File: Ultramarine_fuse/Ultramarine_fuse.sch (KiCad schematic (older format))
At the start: 122 parts, among them J1 Conn_01x04_Female, J2 Conn_01x04_Female, SW1 SW_Push, SW10 SW_Push, SW11 SW_Push, SW12 SW_Push, SW13 SW_Push, SW14 SW_Push, SW15 SW_Push, SW16 SW_Push, SW17 SW_Push, SW18 SW_Push, SW19 SW_Push, SW2 SW_Push, SW20 SW_Push, SW21 SW_Push, SW22 SW_Push, SW23 SW_Push, SW24 SW_Push, SW25 SW_Push, SW26 SW_Push, SW27 SW_Push, SW28 SW_Push, SW29 SW_Push, SW3 SW_Push, SW30 SW_Push, SW31 SW_Push, SW32 SW_Push, SW33 SW_Push, SW34 SW_Push, SW35 SW_Push, SW36 SW_Push, SW4 SW_Push, SW5 SW_Push, SW6 SW_Push, SW7 SW_Push, SW8 SW_Push, SW9 SW_Push, U1 Pro_Micro, U10 SK6812mini, U11 SK6812mini, U12 SK6812mini, U13 SK6812mini, U14 SK6812mini, U15 SK6812mini, U16 SK6812mini, U17 SK6812mini, U18 SK6812mini, U19 SK6812mini, U2 SK6812mini, U20 SK6812mini, U21 SK6812mini, U22 SK6812mini, U23 SK6812mini, U24 SK6812mini, U25 SK6812mini, U26 SK6812mini, U27 SK6812mini, U28 SK6812mini, U29 SK6812mini, U3 SK6812mini, U30 SK6812mini, U31 SK6812mini, U32 SK6812mini, U33 SK6812mini, U34 SK6812mini, U35 SK6812mini, U36 SK6812mini, U4 SK6812mini, U5 SK6812mini, U6 SK6812mini, U7 SK6812mini, U8 SK6812mini, U9 SK6812mini

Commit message: nothing special
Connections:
- net Col0: now also SW1.1, SW15.1, SW22.1, SW8.1
- net Col1: now also SW16.1, SW2.1, SW23.1, SW9.1
- net Col2: now also SW10.1, SW17.1, SW24.1, SW3.1
- net Col3: now also SW11.1, SW18.1, SW25.1, SW4.1
- net Col4: now also SW12.1, SW19.1, SW26.1, SW5.1
- net Col5: now also SW13.1, SW20.1, SW27.1, SW6.1
- net Col6: now also SW14.1, SW21.1, SW28.1, SW7.1
- net GND: now also U10.2 (GND), U11.2 (GND), U12.2 (GND), U13.2 (GND), U14.2 (GND), U15.2 (GND), U23.2 (GND), U24.2 (GND), U25.2 (GND), U26.2 (GND), U27.2 (GND), U28.2 (GND), U29.2 (GND), U31.2 (GND), U32.2 (GND), U33.2 (GND), U34.2 (GND), U35.2 (GND), U36.2 (GND)
- net VCC: now also U10.4 (VCC), U11.4 (VCC), U12.4 (VCC), U13.4 (VCC), U14.4 (VCC), U15.4 (VCC), U23.4 (VCC), U24.4 (VCC), U25.4 (VCC), U26.4 (VCC), U27.4 (VCC), U28.4 (VCC), U29.4 (VCC), U3.4 (VCC), U4.4 (VCC), U5.4 (VCC), U6.4 (VCC), U7.4 (VCC)

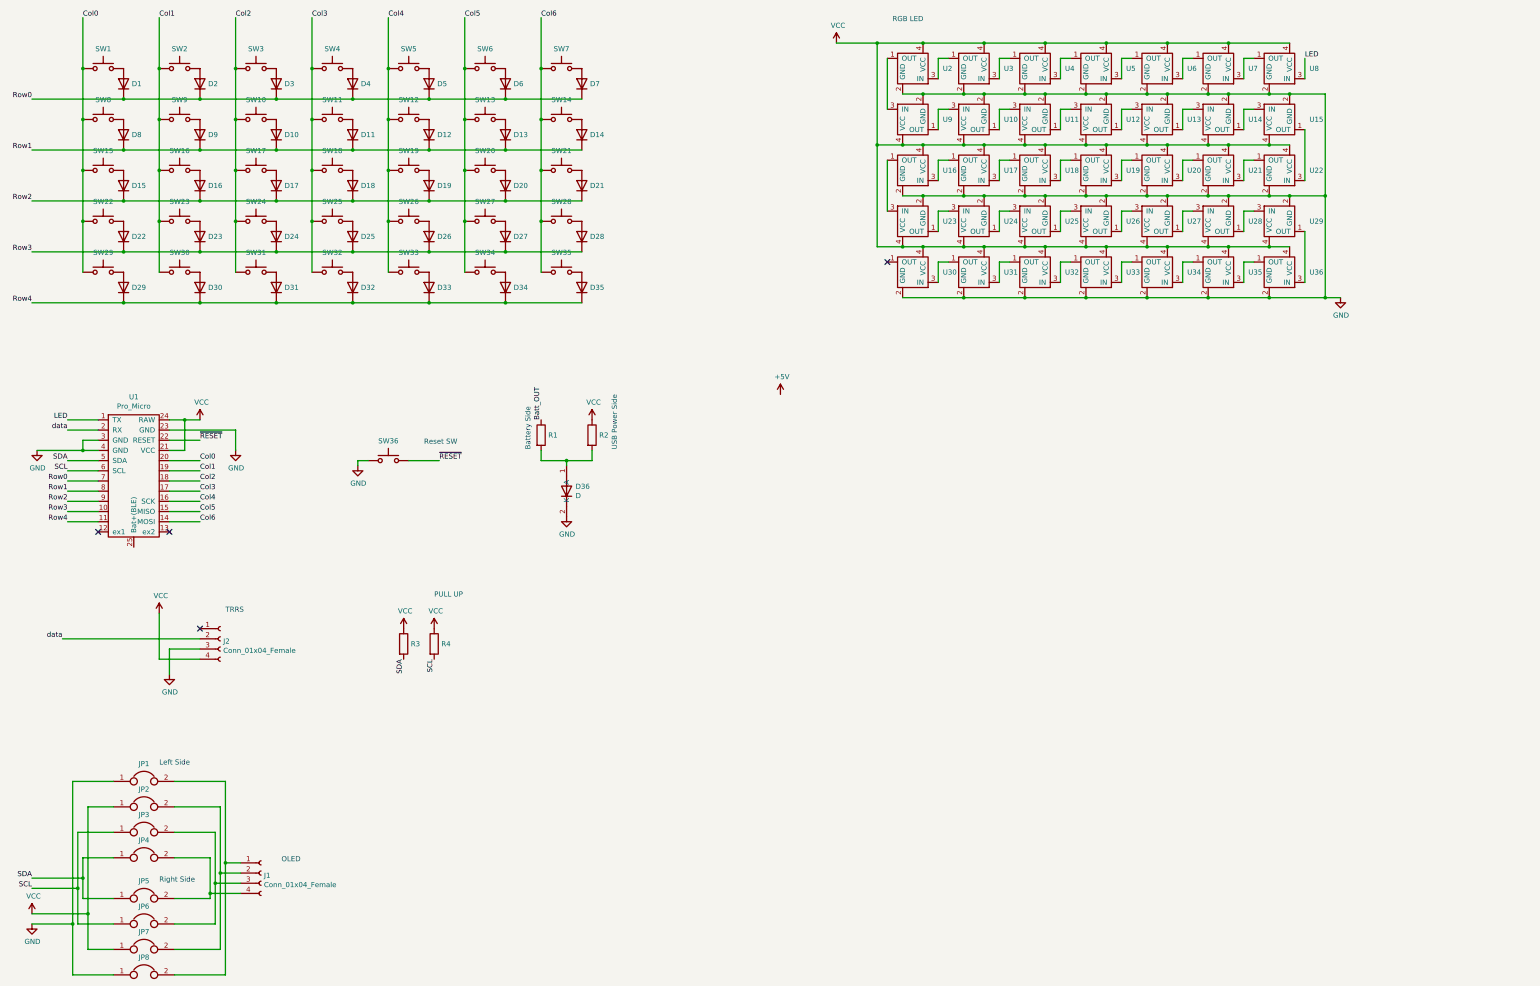
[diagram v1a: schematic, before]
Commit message: PCB making without Charging unit is completed
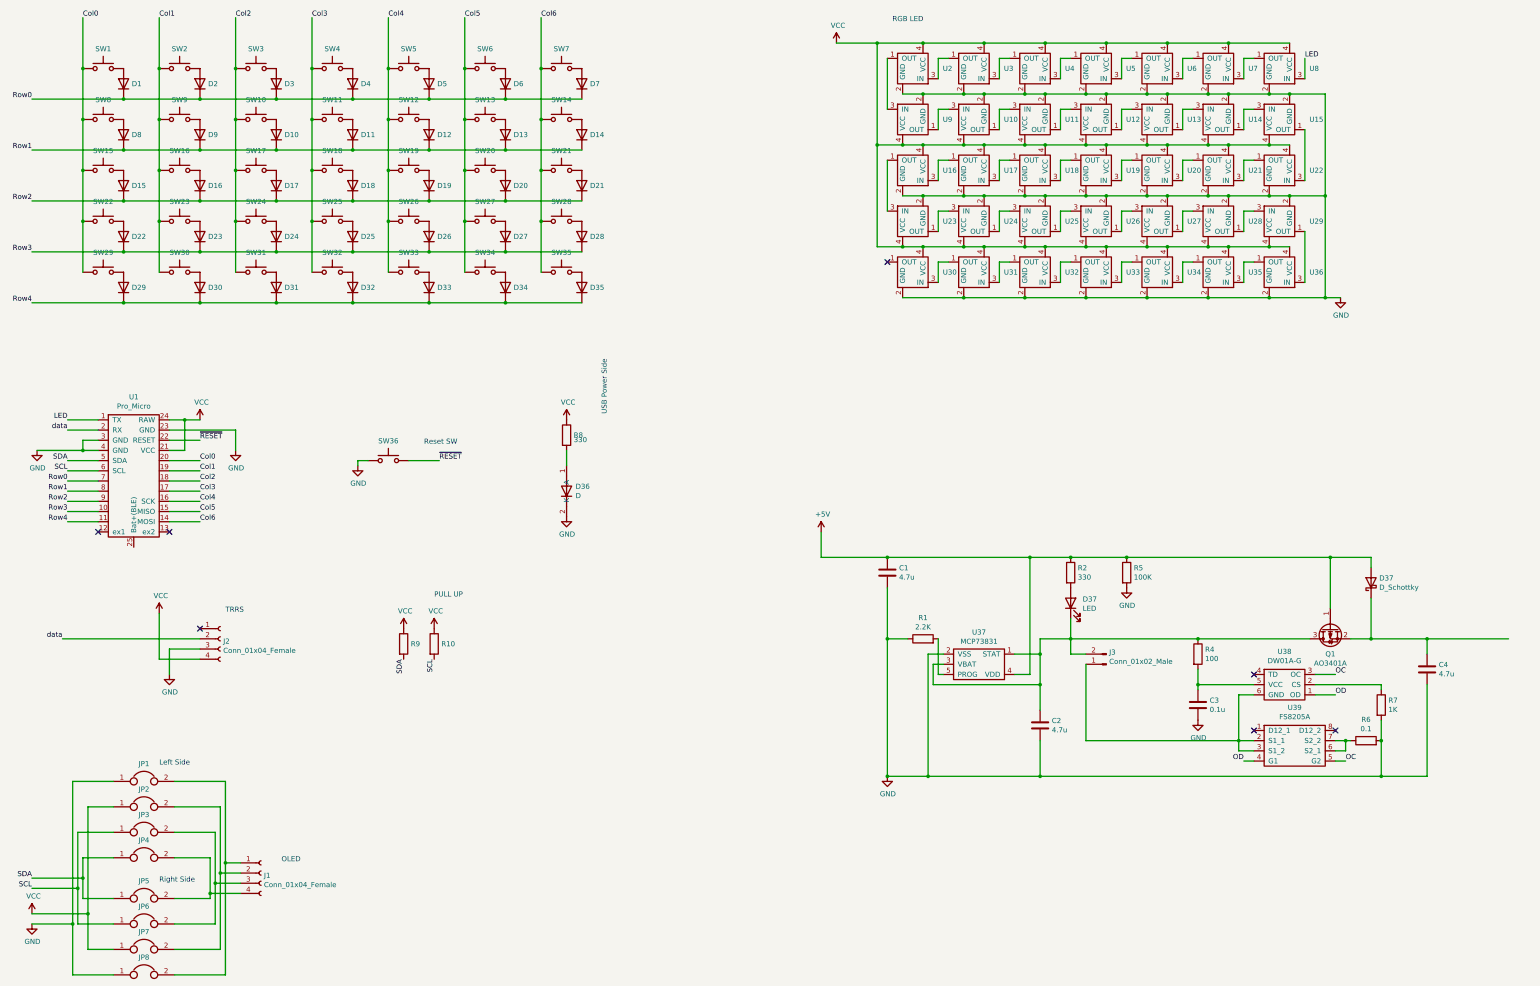
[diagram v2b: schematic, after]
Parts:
- added C1, C2, C4: 4.7u, Basic_SOP:C1608, symbol Device:C
- added C3: 0.1u, Basic_SOP:C1608, symbol Device:C
- added D37: LED, symbol Device:LED
- added D37: D_Schottky, symbol Device:D_Schottky
- added J3: Conn_01x02_Male, symbol Connector:Conn_01x02_Male
- added Q1: AO3401A, Package_TO_SOT_SMD:SOT-23, symbol Transistor_FET:AO3401A
- added R2: 330, Basic_SOP:1608, symbol Device:R
- added R4: 100, Basic_SOP:1608, symbol Device:R
- added R5: 100K, Basic_SOP:1608, symbol Device:R
- added R6: 0.1, Basic_SOP:1608, symbol Device:R
- added R7: 1K, Basic_SOP:1608, symbol Device:R
- added U37: MCP73831, symbol Basic_SOP:MCP73831
- added U38: DW01A-G, symbol Basic_SOP:DW01A-G
- added U39: FS8205A, symbol Basic_SOP:FS8205A
- J1: footprint Connector_PinSocket_2.54mm:PinSocket_1x04_P2.54mm_Vertical -> Basic_THT:4pin_A
- R1: value R -> 2.2K
- R10: renamed from R4; value R -> 10K
- R8: renamed from R2; value R -> 330
- R9: renamed from R3; value R -> 10K
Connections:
- net Batt_OUT is gone; now on net GND: R1.1
- net +5V: now also C1.1, D37.2 (A), Q1.1 (G), R2.1, R5.1, U37.4 (VDD)
- net GND: now also C1.2, C2.2, C3.2, C4.2, R5.2, R6.2, R7.2, U37.2 (VSS)
- net at D36.1 (A), R8.2: no longer R1.2
- new net: C2.1, D37.1 (K), J3.2 (Pin_2), Q1.3 (D), R4.1, U37.1 (STAT), U37.3 (VBAT)
- new net: R1.2, U37.5 (PROG)
- new net: D37.2 (A), R2.2
- new net: C3.1, R4.2, U38.5 (VCC)
- new net: R7.1, U38.2 (CS)
- new net: R6.1, U39.6 (S2_1), U39.7 (S2_2)
- new net: C4.1, D37.1 (K), Q1.2 (S)
- new net: J3.1 (Pin_1), U38.6 (GND), U39.2 (S1_1), U39.3 (S1_2)
- new net OC: U38.3 (OC), U39.5 (G2)
- new net OD: U38.1 (OD), U39.4 (G1)
- no-connect marks 4 -> 7
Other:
- note removed: "Battery Side\n"
- moved on the sheet: R8

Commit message: made for test printing
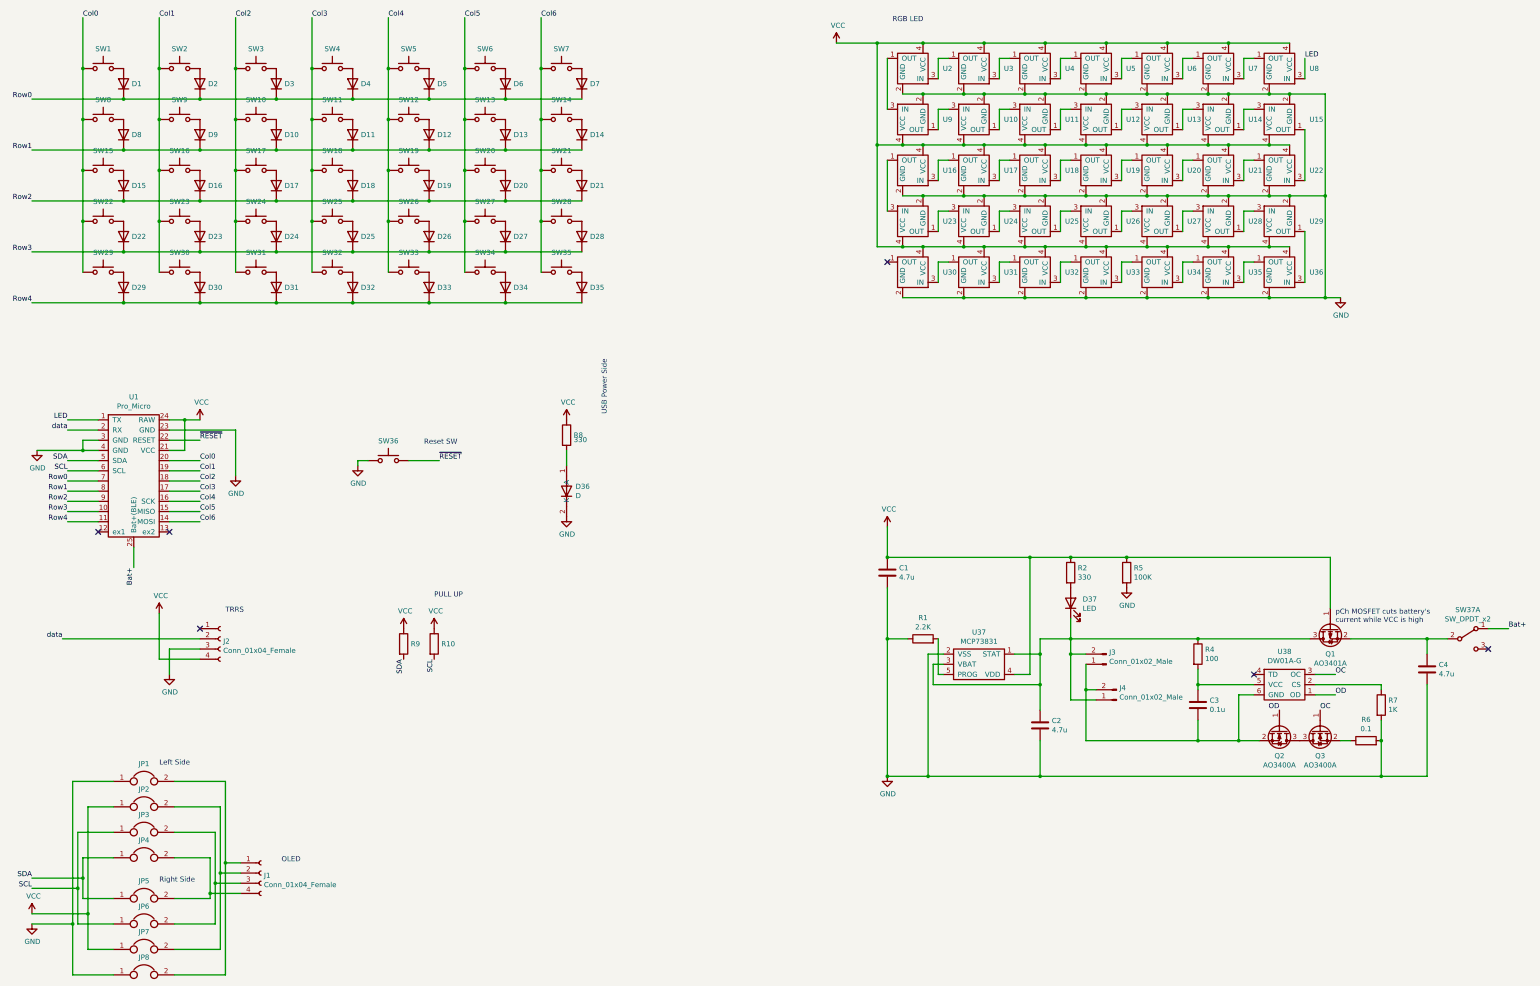
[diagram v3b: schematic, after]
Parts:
- removed D37: D_Schottky, symbol Device:D_Schottky
- removed U39: FS8205A, symbol Basic_SOP:FS8205A
- added J4: Conn_01x02_Male, Basic_THT:S2B-PH-K-S, symbol Connector:Conn_01x02_Male
- added Q2, Q3: AO3400A, Package_TO_SOT_SMD:SOT-23, symbol Transistor_FET:AO3400A
- added SW37: SW_DPDT_x2, Basic_THT:SlideSW-3, symbol Switch:SW_DPDT_x2
- D37: footprint (none) -> Basic_SOP:LED1608
- J3: footprint (none) -> Basic_THT:S2B-PH-K-S
- U37: footprint (none) -> Package_TO_SOT_SMD:SOT-23-5_HandSoldering
- U38: footprint (none) -> Package_TO_SOT_SMD:SOT-23-6_Handsoldering
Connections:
- net +5V is gone; now on net VCC: C1.1, Q1.1 (G), R2.1, R5.1, U37.4 (VDD)
- net GND: no longer C3.2
- net OC: now also Q3.1 (G)
- net OD: now also Q2.1 (G)
- net Bat+: now reaches U1.25 (Bat+(BLE))
- net Bat+: now also SW37.1 (A)
- net at C2.1, D37.1 (K), J3.2 (Pin_2)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: now also J4.1 (Pin_1)
- net at R6.1: now also Q3.2 (S)
- net at C4.1, Q1.2 (S): now also SW37.2 (B)
- net at J3.1 (Pin_1), U38.6 (GND): now also C3.2, J4.2 (Pin_2), Q2.2 (S)
- new net: Q2.3 (D), Q3.3 (D)
- no-connect marks 7 -> 6
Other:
- note added: "pCh MOSFET cuts battery's\ncurrent while VCC is high"
